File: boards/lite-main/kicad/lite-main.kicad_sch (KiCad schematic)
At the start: 145 parts, among them J1 TYPE-C-31-M-12, J2 RCA line in, J3 RCA sub out, J4 DB128V-5.08-4P, Q1 AO4485, Q2 MMBT3904, Q3 MMBT3904, Q4 MMBT3904, SW1 TS-1187A, SW2 TS-1187A, SW3 TS-1187A, U1 CH224A, U2 TPS54302, U3 SY8089A1AAC, U4 LP5907-3.3, U5 ESP32-WROVER-E-N8R8, U6 CH340B, U7 ES8388, U8 TPA3118D2, U9 IRM-3638T

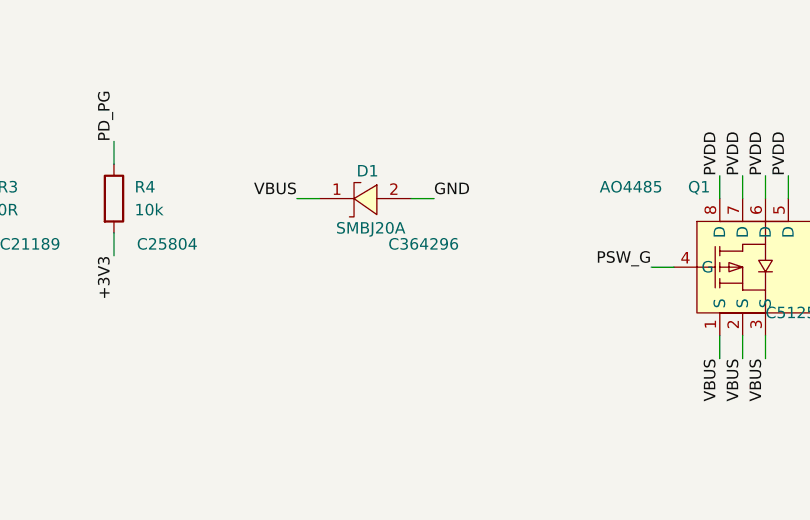
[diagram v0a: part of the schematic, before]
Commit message: Lite's VBUS TVS D1 holds the 21 V PD rail: SMBJ22A (22 V standoff) in place of SMBJ20A, fab and order files regenerated
D1 BORN SMBJ22A C151920, same SMB footprint and pin 1 = K as the MDD SMBJ20A C364296.
Fab BOM/CPL/prebuy and the Digi-Key/Mouser BOMs (stale since the 10-29 ECO) rebuilt
under today's hwde; dfm gate PASS. Ledger: D1 rating verified from BORN's table.
Known unknowns: power:10, thermal:30, parts:45 updated; --check --tier lite 0 open.
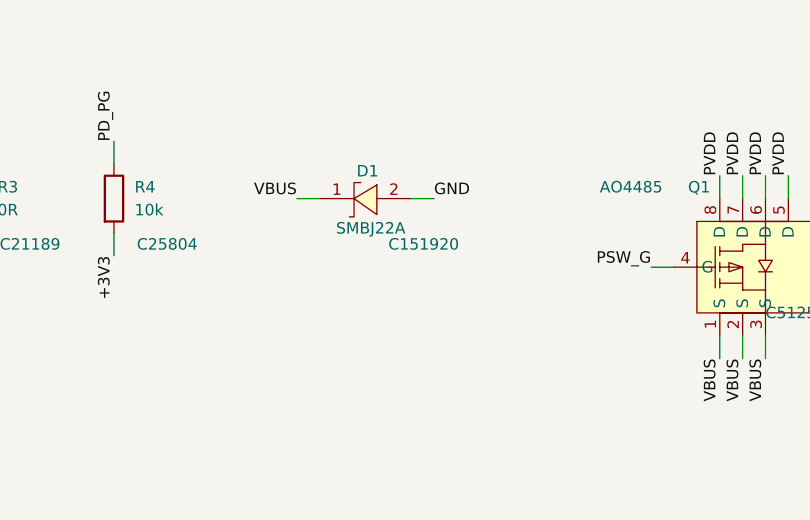
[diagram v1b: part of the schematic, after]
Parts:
- D1: value SMBJ20A -> SMBJ22A; symbol aiee:SMBJ20A_C364296 -> aiee:SMBJ22A_C151920; LCSC C364296 -> C151920
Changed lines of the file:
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@@
 	)
 	(symbol
-		(lib_id "aiee:SMBJ20A_C364296")
+		(lib_id "aiee:SMBJ22A_C151920")
 		(at 320.04 90.17 0)
 		(unit 1)
@@
 			)
 		)
-		(property "Value" "SMBJ20A"
+		(property "Value" "SMBJ22A"
 			(at 316.7646 93.47 0.0000)
 			(effects
@@
 			)
 		)
-		(property "LCSC" "C364296"
+		(property "LCSC" "C151920"
 			(at 322.58 95.2499 0)
 			(effects

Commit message: Lite's sub outs mute on power loss (review-3 R3-AUDIO-2): a +5V sense holds two back-to-back 2N7002s off; when +5V drops they short SUB_L/SUB_R to GND from a 22 uF reservoir for seconds
The as-built thump at a 10k sub input was -1.61 V (full scale); with the mute
it is -25 mV (docs/review-3/sims/fix/lite_mute/tb_powerloss). Off, the gates
sit at Q12's saturation, so the sub line has to stay above -Vth(min) 1.0 V:
firmware caps LOUT2/ROUT2 at -6 dB (0.71 V peak, tb_play_cap; was +4.5 dB).
Q11 is an MMBT3904 as a diode, so no new part numbers beyond the basic
2N7002 (C8545). 9 parts placed in the free pocket under R37-R39 and routed
with miniroute; two GND vias rejoin the pour the new tracks split. DRC clean
(zones refilled), drc_routed and dfm gates pass, fab files regenerated.

Also Lite's thermal governor 13 -> 9 W a channel (R3-LAYOUT-13).
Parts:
- added C90: 22uF, Capacitor_SMD:C_0805_2012Metric, symbol Device:C
- added Q11, Q12: MMBT3904, aiee:SOT-23-3_L2.9-W1.3-P1.90-LS2.4-BR, symbol aiee:MMBT3904-C20526
- added Q13, Q14, Q15: 2N7002, aiee:SOT-23-3_L2.9-W1.3-P1.90-LS2.4-BR, symbol aiee:2N7002
- added R80: 120k, Resistor_SMD:R_0603_1608Metric, symbol Device:R
- added R81: 22k, Resistor_SMD:R_0603_1608Metric, symbol Device:R
- added R82: 47k, Resistor_SMD:R_0603_1608Metric, symbol Device:R
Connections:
- net +5V: now also Q11.1 (B), Q11.3 (C), R80.1
- net GND: now also C90.2, Q12.2 (E), Q14.3 (D), R81.2
- net SUB_L: now also Q13.3 (D)
- net SUB_R: now also Q15.3 (D)
- new net MUTE_DET: Q12.1 (B), R80.2, R81.1
- new net MUTE_RES: C90.1, Q11.2 (E), R82.1
- new net MUTE_S: Q13.2 (S), Q14.2 (S), Q15.2 (S)
- new net SUB_MUTE: Q12.3 (C), Q13.1 (G), Q14.1 (G), Q15.1 (G), R82.2
